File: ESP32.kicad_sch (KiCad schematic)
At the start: 30 parts, among them J201 GPIO, J202 Power, J203 Conn_01x01, J206 IO, J207 Conn_01x07, U201 ESP32-WROOM-32E

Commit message: Rename and update layout
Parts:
- removed D1101, D1102: BAT54A, Package_TO_SOT_SMD:SOT-323_SC-70, symbol Diode:BAT54A
- removed J201: GPIO, Connector_PinHeader_2.54mm:PinHeader_2x20_P2.54mm_Vertical, symbol Connector_Generic:Conn_02x20_Odd_Even
- removed J202: Power, Connector_PinHeader_2.54mm:PinHeader_2x03_P2.54mm_Vertical, symbol Connector_Generic:Conn_02x03_Odd_Even
- removed J203: Conn_01x01, Connector_PinHeader_2.54mm:PinHeader_1x01_P2.54mm_Vertical, symbol Connector_Generic:Conn_01x01
- removed J206: IO, SH-ESP32:PinHeader_1x07_P2.54mm_Vertical-RoundP1, symbol Connector_Generic:Conn_01x07
- removed J207: Conn_01x07, SH-ESP32:PinHeader_1x07_P2.54mm_Vertical-RoundP1, symbol Connector_Generic:Conn_01x07
- removed JP201, JP202, JP203, JP204, JP205, JP206, JP207, JP208, JP209: SolderJumper_2_Open, SH-ESP32:SolderJumper-2_P1.3mm_Open_TrianglePad_Narrow, symbol Jumper:SolderJumper_2_Open
- removed R1103: 10k, Resistor_SMD:R_0402_1005Metric, symbol Device:R
- removed R202, R203, R204, R205, R206, R207, R208, R209, R210: 0R, Resistor_SMD:R_0603_1608Metric, symbol Device:R
- added R302, R303: 2k, Resistor_SMD:R_0402_1005Metric, symbol Device:R
- renumbered C203 to C301, C202 to C302, R201 to R301, U201 to U301
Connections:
- net IO16 is gone; now on net SDA: U301.27 (IO16)
- net IO17 is gone; now on net SCL: U301.28 (IO17)
- net IO34 is gone; now on net CAN_RX: U301.6 (IO34)
- net IO35 is gone; now on net CAN_TX: U301.7 (IO35)
- net +3V3: now also R302.2, R303.2
- net SCL: now also R303.1
- net SDA: now also R302.1
- net IO4 renamed YELLOW_LED
- net LED renamed BLUE_LED
- net RXD0 renamed TXD
- net TXD0 renamed RXD
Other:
- note removed: "0R jumpers allow for rerouting and disabling peripherals"
- note removed: "For safety reasons, a USB 5V two-pin header was downgraded to a single pin test point."
- note removed: "From Espressif Ethernet Reference board"
- note removed: "I2C/LCD"
- note removed: "JTAG"
- note removed: "NOTE: TX/RX Crossover RXD0 -> USB_TXD TXD0 -> USB_RXD"
- note removed: "PHY_MDC"
- note removed: "PHY_MDIO"
- note removed: "PHY_RESET_N"
- note removed: "RMII Ethernet"
- note removed: "RMII_EN"
- note removed: "RMII_RXD0"
- note removed: "RMII_RXD1"
- note removed: "RMII_TXD0"
- note removed: "RMII_TXD1"
- note removed: "RMI_CRS_DV"
- note removed: "Solder jumpers allow for rerouting peripherals GPIOs to J201"
- note removed: "Strap"
- note removed: "UART0"
- title: Sailor Hat with ESP32 -> SH-wg
- moved on the sheet: C301, R301

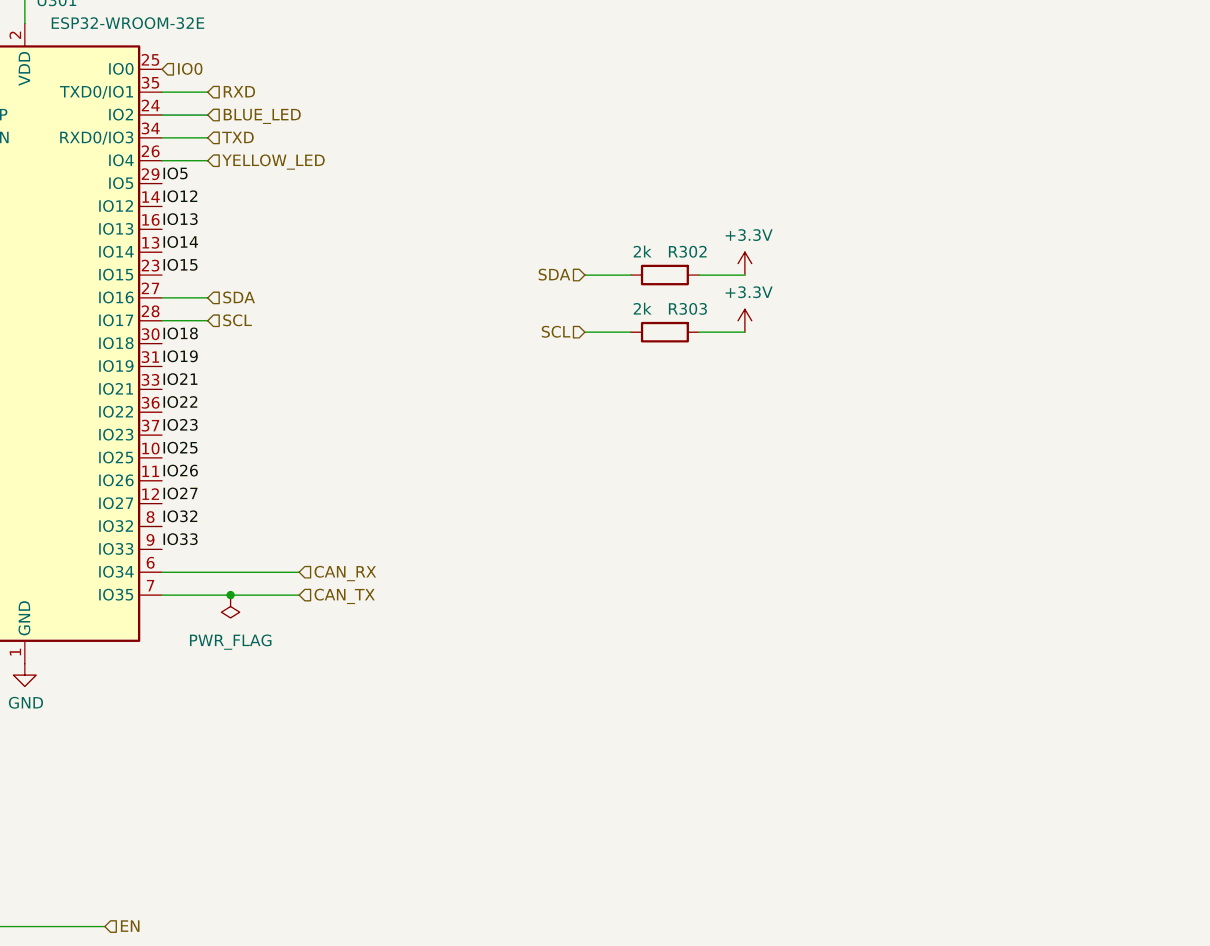
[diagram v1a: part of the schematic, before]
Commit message: Add headers & LEDs
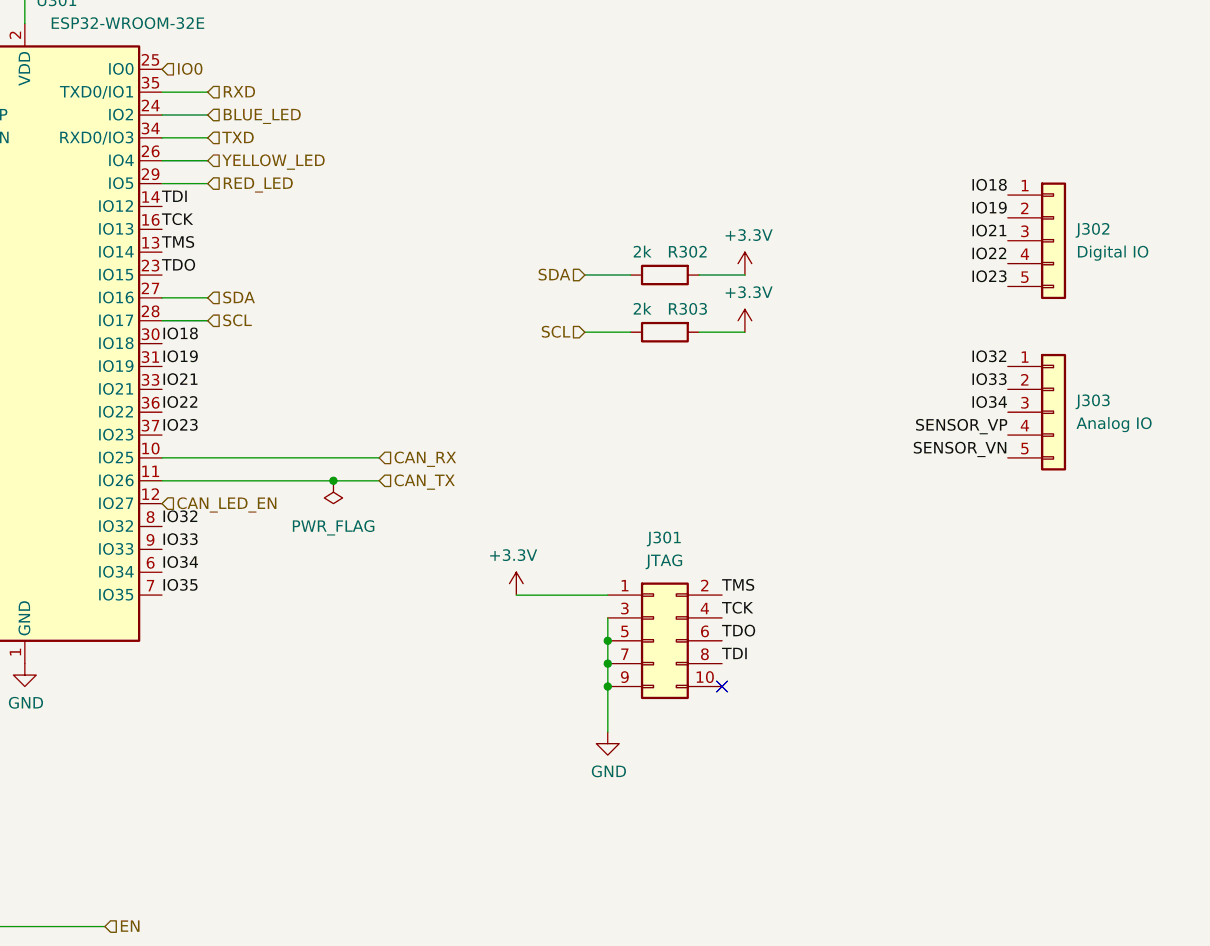
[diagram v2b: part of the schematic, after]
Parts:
- added J301: JTAG, Connector_IDC:IDC-Header_2x05_P2.54mm_Vertical, symbol Connector_Generic:Conn_02x05_Odd_Even
- added J302: Digital IO, Connector_PinHeader_2.54mm:PinHeader_1x05_P2.54mm_Vertical, symbol Connector_Generic:Conn_01x05
- added J303: Analog IO, Connector_PinHeader_2.54mm:PinHeader_1x05_P2.54mm_Vertical, symbol Connector_Generic:Conn_01x05
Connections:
- net IO25 is gone; now on net CAN_RX: U301.10 (IO25)
- net IO26 is gone; now on net CAN_TX: U301.11 (IO26)
- net +3V3: now also J301.1 (Pin_1)
- net CAN_RX: no longer U301.6 (IO34)
- net CAN_TX: no longer U301.7 (IO35)
- net GND: now also J301.3 (Pin_3), J301.5 (Pin_5), J301.7 (Pin_7), J301.9 (Pin_9)
- net IO18: now also J302.1 (Pin_1)
- net IO19: now also J302.2 (Pin_2)
- net IO21: now also J302.3 (Pin_3)
- net IO22: now also J302.4 (Pin_4)
- net IO23: now also J302.5 (Pin_5)
- net IO32: now also J303.1 (Pin_1)
- net IO33: now also J303.2 (Pin_2)
- net SENSOR_VN: now also J303.5 (Pin_5)
- net SENSOR_VP: now also J303.4 (Pin_4)
- net IO12 renamed TDI
- net TDI: now also J301.8 (Pin_8)
- net IO13 renamed TCK
- net TCK: now also J301.4 (Pin_4)
- net IO14 renamed TMS
- net TMS: now also J301.2 (Pin_2)
- net IO15 renamed TDO
- net TDO: now also J301.6 (Pin_6)
- net IO27 renamed CAN_LED_EN
- net IO5 renamed RED_LED
- new net IO34: J303.3 (Pin_3), U301.6 (IO34)
- new net IO35: U301.7 (IO35)
- no-connect marks 6 -> 7

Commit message: Finish 0.1.0 design
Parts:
- J301: LCSC (none) -> C5665
- J302: footprint Connector_PinHeader_2.54mm:PinHeader_1x05_P2.54mm_Vertical -> Connector_PinHeader_2.54mm:PinHeader_1x04_P2.54mm_Vertical; symbol Connector_Generic:Conn_01x05 -> Connector_Generic:Conn_01x04; LCSC (none) -> C358686
- J303: LCSC (none) -> C124379
- U301: footprint SH-ESP32:ESP32-WROOM-32-HandSolder -> SH-wg:ESP32-WROOM-32-HandSolder
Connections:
- net IO19: now also J302.1 (Pin_1); no longer J302.2 (Pin_2)
- net IO21: now also J302.2 (Pin_2); no longer J302.3 (Pin_3)
- net IO22: now also J302.3 (Pin_3); no longer J302.4 (Pin_4)
- net IO23: now also J302.4 (Pin_4); no longer J302.5 (Pin_5)
- net IO18 renamed HALL
- net HALL: no longer J302.1 (Pin_1)
- net RXD renamed ESP_TXD
- net TXD renamed ESP_RXD
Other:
- title: SH-wg -> Sailor Hat WiFi Gateway

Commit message: Chore: C301 value: 1uf -> 1uF
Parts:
- C301: value 1uf -> 1uF
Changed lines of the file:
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@@
       (effects (font (size 1.27 1.27)) (justify left))
     )
-    (property "Value" "1uf" (id 1) (at 57.531 143.383 0)
+    (property "Value" "1uF" (id 1) (at 57.531 143.383 0)
       (effects (font (size 1.27 1.27)) (justify left))
     )
